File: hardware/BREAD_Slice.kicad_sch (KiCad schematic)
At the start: 15 parts, among them J1 Conn_01x10_Female, J2 I2C_01x04

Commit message: Initial commit
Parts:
- removed C1, C3, C4: 22uF, Capacitor_SMD:C_1206_3216Metric, symbol Device:C_Small
- removed C2: 100nF, Capacitor_SMD:C_1206_3216Metric, symbol Device:C_Small
- removed D1: WS2812B_5050, SparkFun-LED:WS2812-5050-4PIN, symbol SparkFun-LED:WS2812B_5050
- removed HS1: Heatsink_Pad, SparkFun-Fuse:Thermal Pad, symbol Mechanical:Heatsink_Pad
- removed J2: I2C_01x04, Connector_JST:JST_SH_SM04B-SRSS-TB_1x04-1MP_P1.00mm_Horizontal, symbol SparkFun-Connector:I2C_01x04
- removed L1: 4.7uH, Inductor_SMD:L_1210_3225Metric, symbol Device:L_Small
- removed U1: ~, Package_TO_SOT_SMD:TSOT-23-6, symbol SparkFun-DiscreteSemi:AP63205
- added C1, C2: 10uF_t, OCI_UPL_FOOTPRINTS:C_2312, symbol BREAD_Slice-rescue:10uF_t-OCI_UPL_2_Capacitors-BREAD_Slice-rescue
- added C3: 10 nF, OCI_UPL_FOOTPRINTS:C_2312, symbol BREAD_Slice-rescue:10uF_t-OCI_UPL_2_Capacitors-BREAD_Slice-rescue
- added C4: 100 nF, Capacitor_SMD:C_1206_3216Metric_Pad1.33x1.80mm_HandSolder, symbol Device:C
- added C5: 100nF_t, Capacitor_SMD:C_1206_3216Metric_Pad1.33x1.80mm_HandSolder, symbol BREAD_Slice-rescue:10uF_t-OCI_UPL_2_Capacitors-BREAD_Slice-rescue
- added FB1: Ferrite_Bead, OCI_UPL_FOOTPRINTS:R_1206_HandSoldering, symbol BREAD_Slice-rescue:Ferrite_Bead-Device
- added J2, J3: USB_A, Connector_USB:USB_A_Molex_67643_Horizontal, symbol Connector:USB_A
- added Logo1: Logo_Open_Hardware_Small, Symbol:OSHW-Symbol_6.7x6mm_SilkScreen, symbol Graphic:Logo_Open_Hardware_Small
- added R1: 10k, OCI_UPL_FOOTPRINTS:R_1206_HandSoldering, symbol Device:R
- added R2: 1k, Resistor_SMD:R_1206_3216Metric_Pad1.30x1.75mm_HandSolder, symbol Device:R_US
- added U1: FSUSB42MUX, Package_SO:MSOP-10_3x3mm_P0.5mm, symbol Interface_USB:FSUSB42MUX
- added U2: FT232RL, Package_SO:SSOP-28_5.3x10.2mm_P0.65mm, symbol Interface_USB:FT232RL
- H1, H4: footprint MountingHole:MountingHole_5mm -> MountingHole:MountingHole_3.2mm_M3_DIN965_Pad
- H2: renamed from H3; footprint MountingHole:MountingHole_5mm -> MountingHole:MountingHole_3.2mm_M3_DIN965_Pad
- H3: renamed from H2; footprint MountingHole:MountingHole_5mm -> MountingHole:MountingHole_3.2mm_M3_DIN965_Pad
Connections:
- net +12V: now also A1.30 (VIN), C1.1
- net +5V: now also C2.1, FB1.1, R1.1, U1.1 (VCC), U2.20 (VCC), U2.4 (VCCIO)
- net GND: now also C1.2, C2.2, C3.2, C4.1, J2.4 (GND), J2.5 (Shield), J3.4 (GND), J3.5 (Shield), U1.10 (~{OE}), U1.5 (GND), U2.18 (GND), U2.21 (GND), U2.25 (AGND), U2.26 (TEST), U2.7 (GND)
- net TR: now reaches A1.1 (D1/TX)
- net TR: now also U2.1 (TXD)
- net SEL: now reaches A1.10 (D7)
- net SEL: now also U1.2 (SEL)
- net PWREN: now reaches A1.11 (D8)
- net PWREN: now also R1.2, U2.14 (CBUS3)
- net RT: now reaches A1.2 (D0/RX)
- net RT: now also U2.5 (RXD)
- net RESET: now reaches A1.28 (~{RESET})
- net RESET: now also C5.1
- net LED: no longer names the net of A1.8 (D5)
- new net: C3.1, FB1.2, J2.1 (VBUS), J3.1 (VBUS)
- new net: J3.2 (D-), U1.8 (HSD2-)
- new net: J3.3 (D+), U1.9 (HSD2+)
- new net: C4.2, U2.17 (3V3OUT)
- new net: C5.2, R2.2, U2.2 (DTR)
- new net: R2.1, U2.3 (RTS)
- new net: J2.2 (D-), U1.6 (HSD1-)
- new net: J2.3 (D+), U1.7 (HSD1+)
- new net D+: U1.3 (D+), U2.15 (USBD+)
- new net D-: U1.4 (D-), U2.16 (USBD-)
- no-connect marks 22 -> 27
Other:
- moved on the sheet: A1, H1, H2, H3, H4, J1

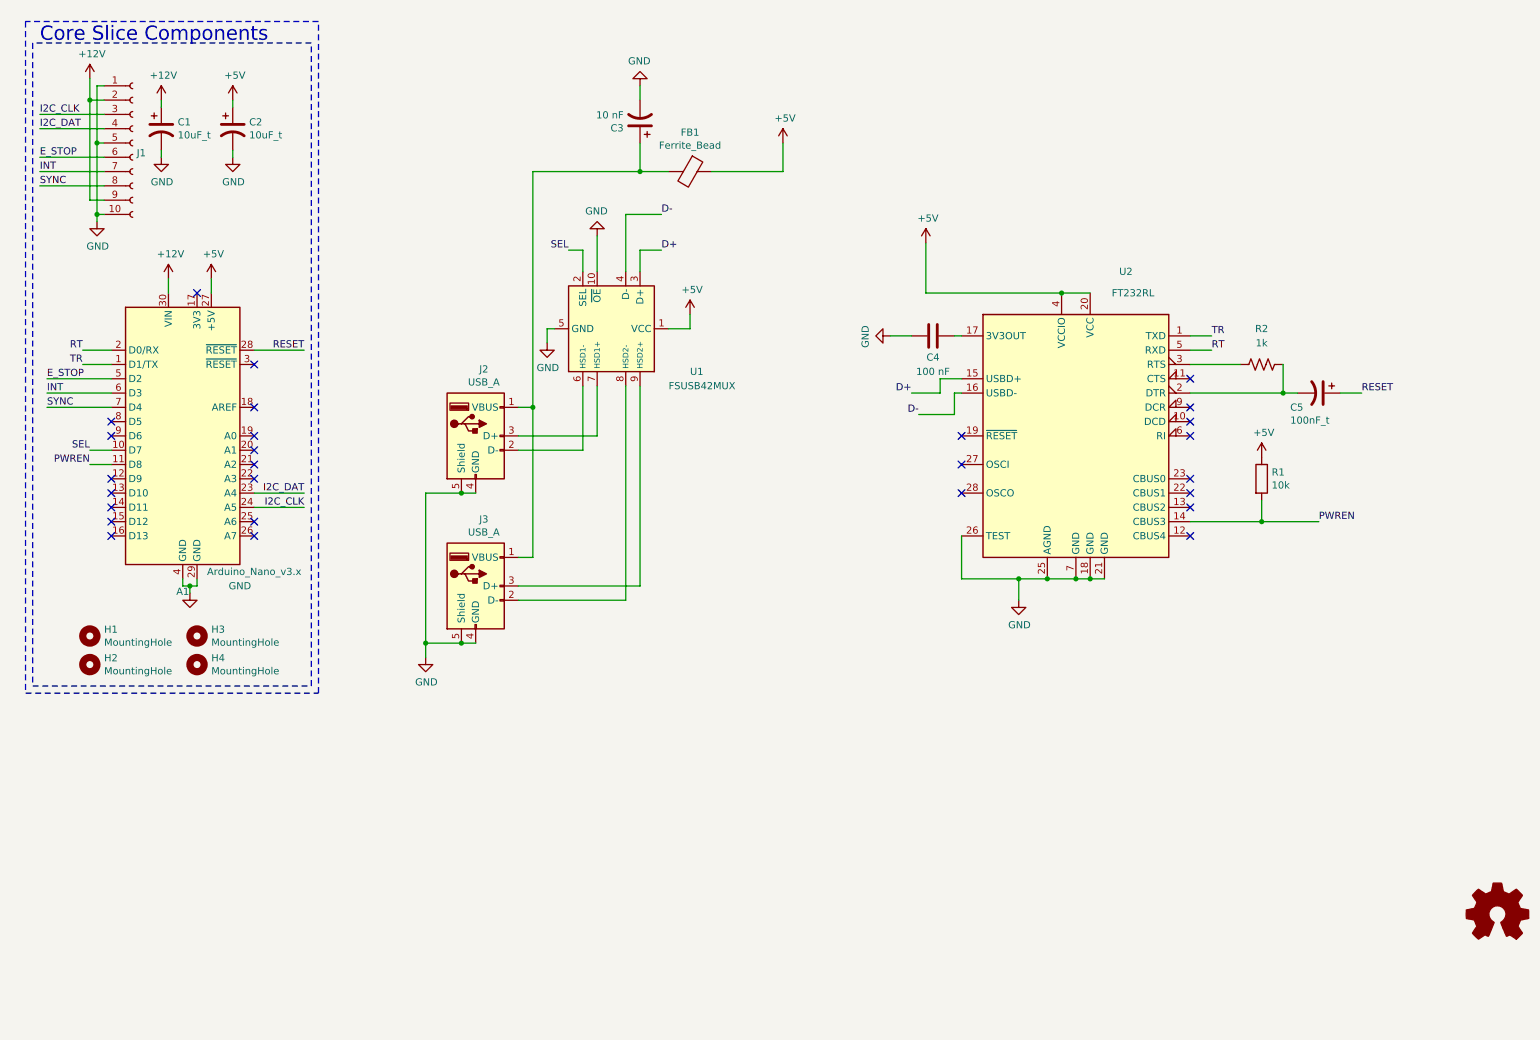
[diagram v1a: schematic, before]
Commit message: optimized pcb and updated to new core
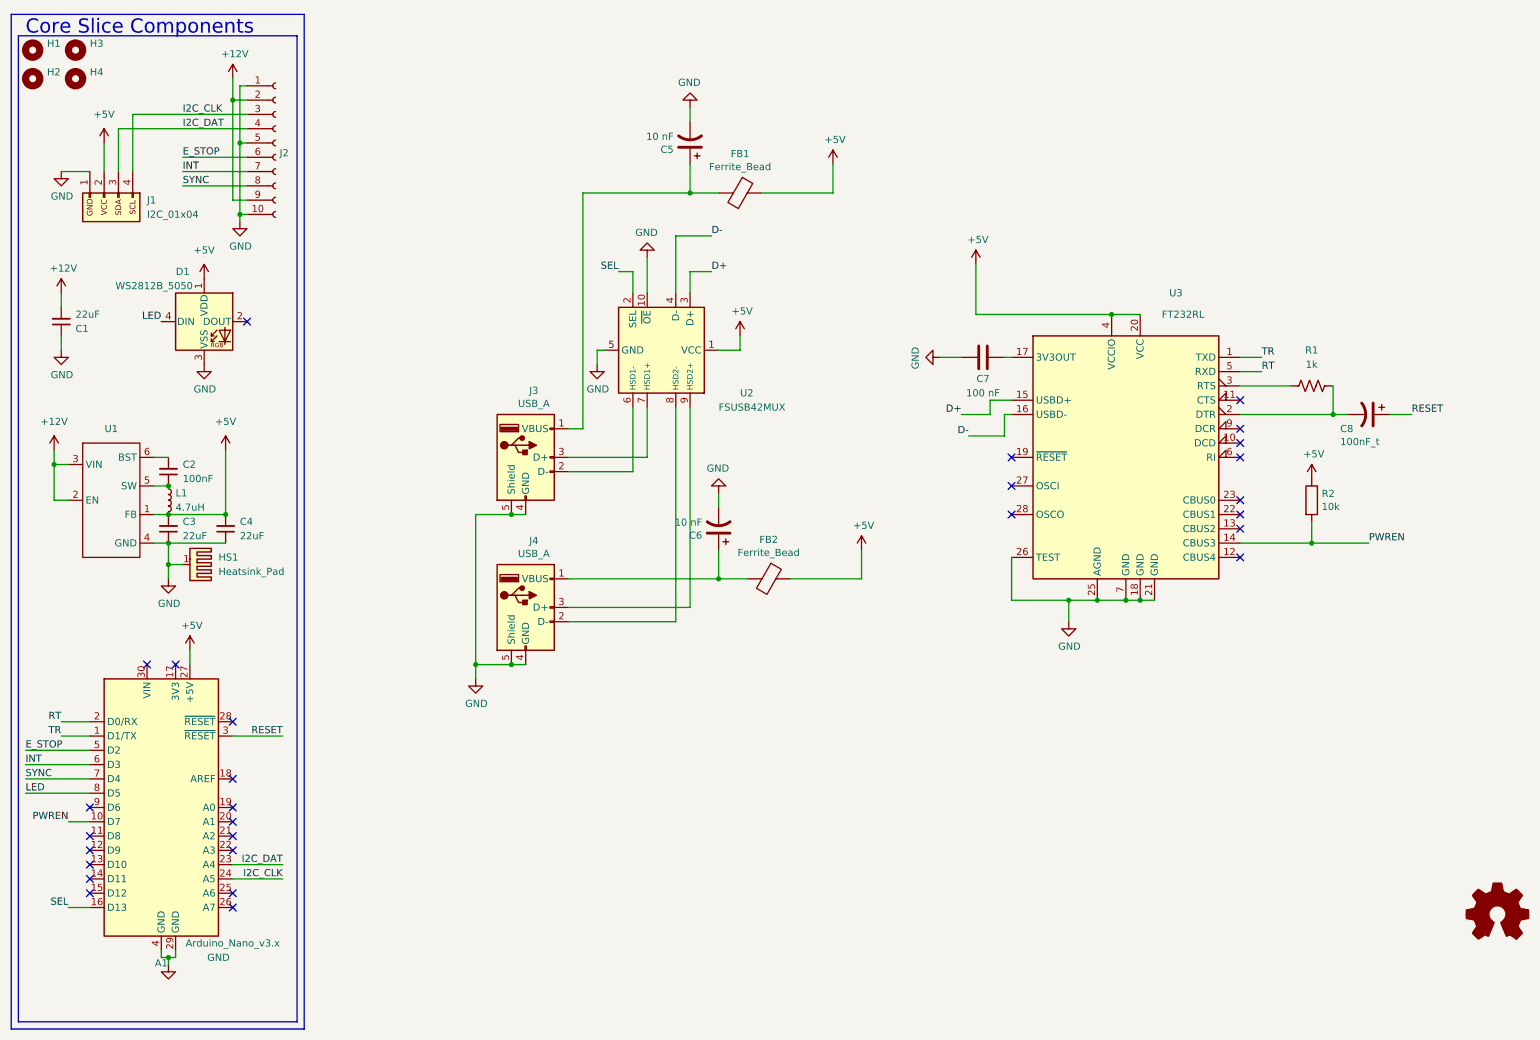
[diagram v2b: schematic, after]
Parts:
- removed C1, C2: 10uF_t, OCI_UPL_FOOTPRINTS:C_2312, symbol BREAD_Slice-rescue:10uF_t-OCI_UPL_2_Capacitors-BREAD_Slice-rescue
- removed C3: 10 nF, OCI_UPL_FOOTPRINTS:C_2312, symbol BREAD_Slice-rescue:10uF_t-OCI_UPL_2_Capacitors-BREAD_Slice-rescue
- removed C4: 100 nF, Capacitor_SMD:C_1206_3216Metric_Pad1.33x1.80mm_HandSolder, symbol Device:C
- removed J2: USB_A, Connector_USB:USB_A_Molex_67643_Horizontal, symbol Connector:USB_A
- removed Logo1: Logo_Open_Hardware_Small, Symbol:OSHW-Symbol_6.7x6mm_SilkScreen, symbol Graphic:Logo_Open_Hardware_Small
- removed R1: 10k, OCI_UPL_FOOTPRINTS:R_1206_HandSoldering, symbol Device:R
- removed R2: 1k, Resistor_SMD:R_1206_3216Metric_Pad1.30x1.75mm_HandSolder, symbol Device:R_US
- removed U1: FSUSB42MUX, Package_SO:MSOP-10_3x3mm_P0.5mm, symbol Interface_USB:FSUSB42MUX
- removed U2: FT232RL, Package_SO:SSOP-28_5.3x10.2mm_P0.65mm, symbol Interface_USB:FT232RL
- added C1, C3, C4: 22uF, Capacitor_SMD:C_1206_3216Metric_Pad1.33x1.80mm_HandSolder, symbol Device:C_Small
- added C2: 100nF, Capacitor_SMD:C_1206_3216Metric_Pad1.33x1.80mm_HandSolder, symbol Device:C_Small
- added C6: 10 nF, Capacitor_SMD:C_1206_3216Metric_Pad1.33x1.80mm_HandSolder, symbol BREAD_Slice-rescue:10uF_t-OCI_UPL_2_Capacitors-BREAD_Slice-rescue
- added C7: 100 nF, Capacitor_SMD:C_1206_3216Metric_Pad1.33x1.80mm_HandSolder, symbol Device:C
- added C8: 100nF_t, Capacitor_SMD:C_1206_3216Metric_Pad1.33x1.80mm_HandSolder, symbol BREAD_Slice-rescue:10uF_t-OCI_UPL_2_Capacitors-BREAD_Slice-rescue
- added D1: WS2812B_5050, SparkFun-LED:WS2812-5050-4PIN, symbol SparkFun-LED:WS2812B_5050
- added FB2: Ferrite_Bead, Resistor_SMD:R_1206_3216Metric_Pad1.30x1.75mm_HandSolder, symbol BREAD_Slice-rescue:Ferrite_Bead-Device
- added HS1: Heatsink_Pad, KML-Custom:Thermal Pad, symbol Mechanical:Heatsink_Pad
- added J1: I2C_01x04, Connector_JST:JST_SH_SM04B-SRSS-TB_1x04-1MP_P1.00mm_Horizontal, symbol SparkFun-Connector:I2C_01x04
- added J4: USB_A, Connector_USB:USB_A_Molex_67643_Horizontal, symbol Connector:USB_A
- added L1: 4.7uH, Inductor_SMD:L_1210_3225Metric, symbol Device:L_Small
- added R1: 1k, Resistor_SMD:R_1206_3216Metric_Pad1.30x1.75mm_HandSolder, symbol Device:R_US
- added R2: 10k, Resistor_SMD:R_1206_3216Metric_Pad1.30x1.75mm_HandSolder, symbol Device:R
- added U1: ~, Package_TO_SOT_SMD:TSOT-23-6, symbol SparkFun-DiscreteSemi:AP63205
- added U2: FSUSB42MUX, Package_SO:MSOP-10_3x3mm_P0.5mm, symbol Interface_USB:FSUSB42MUX
- added U3: FT232RL, Package_SO:SSOP-28_5.3x10.2mm_P0.65mm, symbol Interface_USB:FT232RL
- C5: value 100nF_t -> 10 nF
- FB1: footprint OCI_UPL_FOOTPRINTS:R_1206_HandSoldering -> Resistor_SMD:R_1206_3216Metric_Pad1.30x1.75mm_HandSolder
- H1, H4: footprint MountingHole:MountingHole_3.2mm_M3_DIN965_Pad -> MountingHole:MountingHole_5mm
- H2: renamed from H3; footprint MountingHole:MountingHole_3.2mm_M3_DIN965_Pad -> MountingHole:MountingHole_5mm
- H3: renamed from H2; footprint MountingHole:MountingHole_3.2mm_M3_DIN965_Pad -> MountingHole:MountingHole_5mm
- renumbered J1 to J2
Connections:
- net +12V: now also C1.2, U1.2 (EN), U1.3 (VIN); no longer A1.30 (VIN)
- net +5V: now also C3.2, C4.2, D1.1 (VDD), FB2.1, J1.2 (Pin_2), L1.2, R2.1, U1.1 (FB), U2.1 (VCC), U3.20 (VCC), U3.4 (VCCIO)
- net D+: now also U2.3 (D+), U3.15 (USBD+)
- net D-: now also U2.4 (D-), U3.16 (USBD-)
- net GND: now also C5.2, C1.1, C3.1, C4.1, C6.2, C7.1, D1.3 (VSS), HS1.1, J1.1 (Pin_1), J4.4 (GND), J4.5 (Shield), U1.4 (GND), U2.10 (~{OE}), U2.5 (GND), U3.18 (GND), U3.21 (GND), U3.25 (AGND), U3.26 (TEST), U3.7 (GND)
- net I2C_CLK: now also J1.4 (Pin_4)
- net I2C_DAT: now also J1.3 (Pin_3)
- net PWREN: now also A1.10 (D7), R2.2, U3.14 (CBUS3); no longer A1.11 (D8)
- net RESET: now also A1.3 (~{RESET}), C8.1; no longer A1.28 (~{RESET}), C5.1
- net RT: now also U3.5 (RXD)
- net SEL: now also A1.16 (D13), U2.2 (SEL); no longer A1.10 (D7)
- net TR: now also U3.1 (TXD)
- net LED: now reaches A1.8 (D5)
- net LED: now also D1.4 (DIN)
- net at FB1.2, J3.1 (VBUS): now also C5.1
- net at J3.2 (D-): now also U2.6 (HSD1-)
- net at J3.3 (D+): now also U2.7 (HSD1+)
- new net: C8.2, R1.2, U3.2 (DTR)
- new net: C6.1, FB2.2, J4.1 (VBUS)
- new net: J4.2 (D-), U2.8 (HSD2-)
- new net: J4.3 (D+), U2.9 (HSD2+)
- new net: C2.1, L1.1, U1.5 (SW)
- new net: C2.2, U1.6 (BST)
- new net: R1.1, U3.3 (RTS)
- new net: C7.2, U3.17 (3V3OUT)
- no-connect marks 27 -> 28
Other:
- moved on the sheet: A1, H1, H2, H3, H4, J2
